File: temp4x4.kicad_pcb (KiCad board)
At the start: 2 copper layers, 51.8 x 26.4 mm, 45 parts, among them J1 RTD1, J2 NUCLEO_CN6_1-6, J3 RTD1, J4 NUCLEO_CN5_10-1, J5 RTD1, J6 RTD1, U1 LP5907MFX-3.3_NOPB, U2 ADS124S08IPBS

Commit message: re-done layout
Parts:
- moved C15 0.79 mm to (130.3, 135.1), turned to 270 degrees
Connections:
- C2 pad 2: Net-(C2-Pad2) -> Earth
- U1 pad 2: Net-(C2-Pad2) -> Earth
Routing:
- net Earth: track 0.00 -> 195.9 mm, vias 0 -> 3
- net ENABLE: track 0.00 -> 68.9 mm, vias 0 -> 2
- net Net-(J1-Pad1): track 0.00 -> 51.1 mm, vias 0 -> 1
- net Net-(J6-Pad4): track 0.00 -> 40.3 mm
- net Net-(C19-Pad1): track 0.00 -> 35.6 mm
- net IOREF: track 0.00 -> 34.5 mm, vias 0 -> 2
- net Net-(J1-Pad4): track 0.00 -> 29.2 mm
- net Net-(J3-Pad4): track 0.00 -> 29.1 mm
- net +5V: track 0.00 -> 27.2 mm, vias 0 -> 1
- net +3V3: track 0.00 -> 26.4 mm, vias 0 -> 2
- net Net-(C5-Pad1): track 0.00 -> 25.8 mm, vias 0 -> 1
- net DRDY: track 0.00 -> 25.4 mm, vias 0 -> 1
- net Net-(C13-Pad1): track 0.00 -> 25.0 mm, vias 0 -> 1
- net Net-(C7-Pad1): track 0.00 -> 23.9 mm, vias 0 -> 1
- net Net-(C12-Pad1): track 0.00 -> 22.9 mm, vias 0 -> 1
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
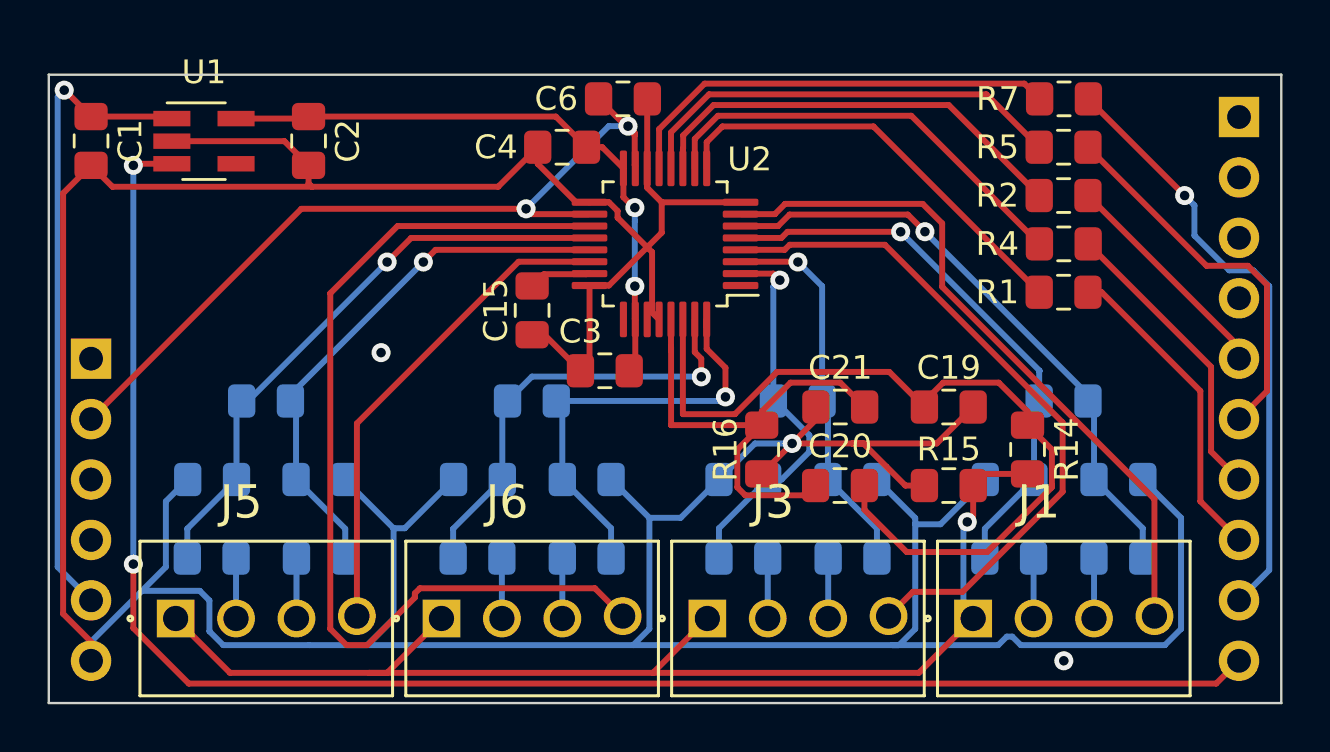
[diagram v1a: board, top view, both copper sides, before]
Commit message: added silkscreen labels
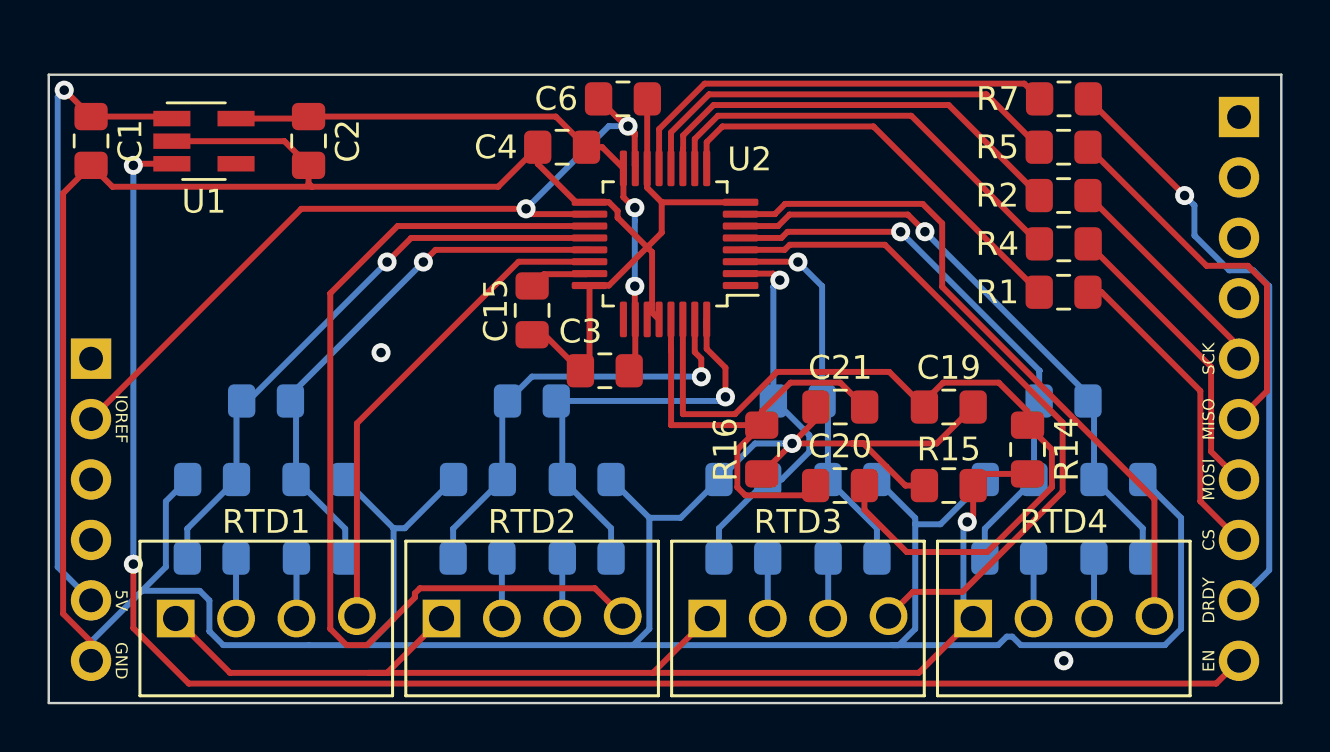
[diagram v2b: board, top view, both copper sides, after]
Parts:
- J1: value RTD1 -> RTD4
- J3: value RTD1 -> RTD3
- J6: value RTD1 -> RTD2
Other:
- board text added: "5V"
- board text added: "CS"
- board text added: "DRDY"
- board text added: "EN"
- board text added: "GND"
- board text added: "IOREF"
- board text added: "MISO"
- board text added: "MOSI"
- board text added: "SCK"

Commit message: added OSHW logo
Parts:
- added G***: LOGO, temp4x4:oshw_logo, F.Cu at (119.1, 138.6)
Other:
- board text added: "temp4x4"

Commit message: some PCB fine tuning
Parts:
- moved G*** 0.32 mm to (118.8, 138.7)
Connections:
- J2 pad 1: Net-(J2-Pad1) -> (no net)
- J2 pad 3: Net-(J2-Pad3) -> (no net)
- J2 pad 4: Net-(J2-Pad4) -> (no net)
- J4 pad 1: Net-(J4-Pad1) -> (no net)
- J4 pad 2: Net-(J4-Pad2) -> (no net)
- J4 pad 3: Net-(J4-Pad3) -> (no net)
- J4 pad 4: Net-(J4-Pad4) -> (no net)
- U2 pad 1: Net-(U2-Pad1) -> (no net)
- U2 pad 25: Net-(U2-Pad25) -> (no net)
